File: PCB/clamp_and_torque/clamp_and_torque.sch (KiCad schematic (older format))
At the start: 12 parts, among them J1 Servo1, J2 Servo2, J3 LimitSwitches, J4 Conn_01x02_Female, J5 Conn_01x02_Female

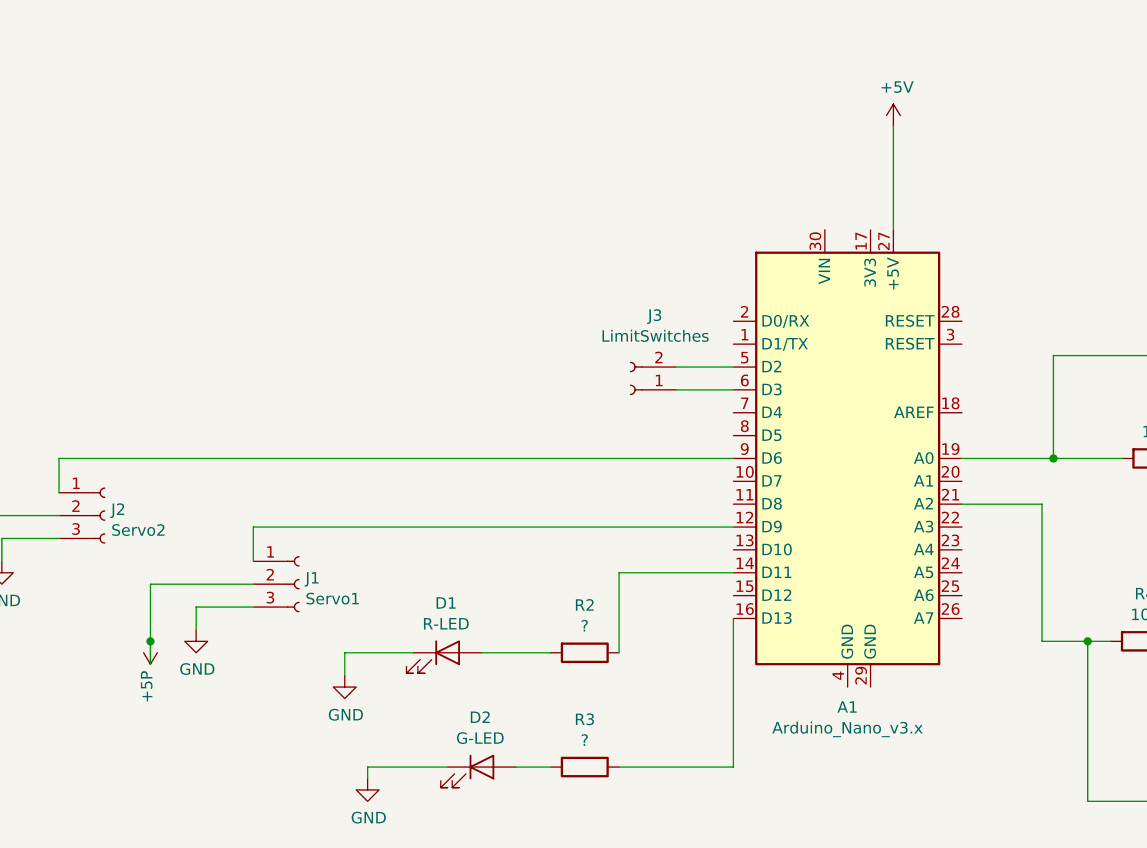
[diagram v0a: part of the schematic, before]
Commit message: Update some footprints and add a few more components.
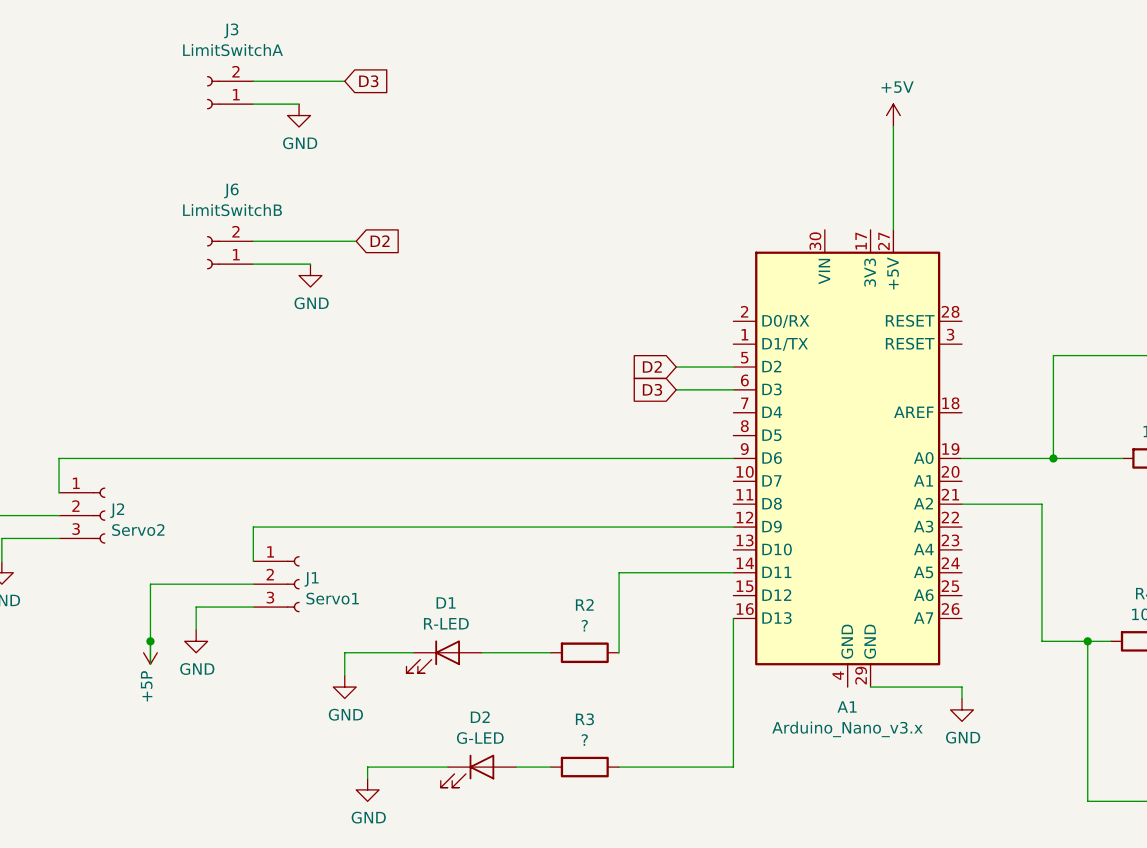
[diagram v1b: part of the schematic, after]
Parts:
- added J6: LimitSwitchB, Connector_PinHeader_2.54mm:PinHeader_1x02_P2.54mm_Vertical, symbol Connector:Conn_01x02_Female
- J1, J2: footprint (none) -> Connector_PinHeader_2.54mm:PinHeader_1x02_P5.04mm_Vertical
- J3: value LimitSwitches -> LimitSwitchA
- J4, J5: footprint (none) -> Connector_PinHeader_2.54mm:PinHeader_1x02_P2.54mm_Vertical_V2
- R1, R4: footprint (none) -> Resistor_SMD:R_0603_1608Metric
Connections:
- net labels added: D2, D3
- wire segments 45 -> 51
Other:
- moved on the sheet: J3
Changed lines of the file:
@@
 EESchema Schematic File Version 4
+LIBS:clamp_and_torque-cache
 EELAYER 30 0
 EELAYER END
@@
 F 0 "R1" V 6243 3550 50  0000 C CNN
 F 1 "10k" V 6334 3550 50  0000 C CNN
-F 2 "" H 6520 3459 50  0000 L CNN
+F 2 "Resistor_SMD:R_0603_1608Metric" H 6520 3459 50  0001 L CNN
 F 3 "~" H 6450 3550 50  0001 C CNN
 	1    6450 3550
@@
 F 0 "J1" H 2728 4126 50  0000 L CNN
 F 1 "Servo1" H 2728 4035 50  0000 L CNN
-F 2 "" H 2700 4100 50  0001 C CNN
+F 2 "Connector_PinHeader_2.54mm:PinHeader_1x02_P5.04mm_Vertical" H 2700 4100 50  0001 C CNN
 F 3 "~" H 2700 4100 50  0001 C CNN
 	1    2700 4100
@@
 F 0 "J4" H 7478 2976 50  0000 L CNN
 F 1 "Conn_01x02_Female" H 7478 2885 50  0000 L CNN
-F 2 "" H 7450 3000 50  0001 C CNN
+F 2 "Connector_PinHeader_2.54mm:PinHeader_1x02_P2.54mm_Vertical_V2" H 7450 3000 50  0001 C CNN
 F 3 "~" H 7450 3000 50  0001 C CNN
 	1    7450 3000
@@
 L Connector:Conn_01x02_Female J3
 U 1 1 5DAFAF0D
-P 4150 3250
-F 0 "J3" H 4042 2925 50  0000 C CNN
-F 1 "LimitSwitches" H 4042 3016 50  0000 C CNN
-F 2 "Connector_PinHeader_2.54mm:PinHeader_1x02_P2.54mm_Vertical" H 4150 3250 50  0001 C CNN
-F 3 "~" H 4150 3250 50  0001 C CNN
-	1    4150 3250
+P 2300 2000
+F 0 "J3" H 2192 1675 50  0000 C CNN
+F 1 "LimitSwitchA" H 2192 1766 50  0000 C CNN
+F 2 "Connector_PinHeader_2.54mm:PinHeader_1x02_P2.54mm_Vertical" H 2300 2000 50  0001 C CNN
+F 3 "~" H 2300 2000 50  0001 C CNN
+	1    2300 2000
 	-1   0    0    1
 $EndComp
@@
 F 0 "J2" H 1878 3826 50  0000 L CNN
 F 1 "Servo2" H 1878 3735 50  0000 L CNN
-F 2 "" H 1850 3800 50  0001 C CNN
+F 2 "Connector_PinHeader_2.54mm:PinHeader_1x02_P5.04mm_Vertical" H 1850 3800 50  0001 C CNN
 F 3 "~" H 1850 3800 50  0001 C CNN
 	1    1850 3800
@@
 F 0 "J5" H 7628 4926 50  0000 L CNN
 F 1 "Conn_01x02_Female" H 7628 4835 50  0000 L CNN
-F 2 "" H 7600 4950 50  0001 C CNN
+F 2 "Connector_PinHeader_2.54mm:PinHeader_1x02_P2.54mm_Vertical_V2" H 7600 4950 50  0001 C CNN
 F 3 "~" H 7600 4950 50  0001 C CNN
 	1    7600 4950
@@
 F 0 "R4" V 6193 4350 50  0000 C CNN
 F 1 "10k" V 6284 4350 50  0000 C CNN
-F 2 "" H 6470 4259 50  0000 L CNN
+F 2 "Resistor_SMD:R_0603_1608Metric" H 6470 4259 50  0001 L CNN
 F 3 "~" H 6400 4350 50  0001 C CNN
 	1    6400 4350
@@
 Wire Wire Line
 	6150 5050 7400 5050
+$Comp
+L Connector:Conn_01x02_Female J6
+U 1 1 5DB0E066
+P 2300 2700
+F 0 "J6" H 2192 2375 50  0000 C CNN
+F 1 "LimitSwitchB" H 2192 2466 50  0000 C CNN
+F 2 "Connector_PinHeader_2.54mm:PinHeader_1x02_P2.54mm_Vertical" H 2300 2700 50  0001 C CNN
+F 3 "~" H 2300 2700 50  0001 C CNN
+	1    2300 2700
+	-1   0    0    1
+$EndComp
+$Comp
+L power:GND #PWR0112
+U 1 1 5DB0EAAF
+P 2700 2000
+F 0 "#PWR0112" H 2700 1750 50  0001 C CNN
+F 1 "GND" H 2705 1827 50  0000 C CNN
+F 2 "" H 2700 2000 50  0001 C CNN
+F 3 "" H 2700 2000 50  0001 C CNN
+	1    2700 2000
+	1    0    0    -1
+$EndComp
+Text GLabel 4350 3150 0    50   Input ~ 0
+D2
+Text GLabel 4350 3250 0    50   Input ~ 0
+D3
+Text GLabel 2950 2600 2    50   Input ~ 0
+D2
+Text GLabel 2900 1900 2    50   Input ~ 0
+D3
+$Comp
+L power:GND #PWR0113
+U 1 1 5DB1DE6D
+P 2750 2700
+F 0 "#PWR0113" H 2750 2450 50  0001 C CNN
+F 1 "GND" H 2755 2527 50  0000 C CNN
+F 2 "" H 2750 2700 50  0001 C CNN
+F 3 "" H 2750 2700 50  0001 C CNN
+	1    2750 2700
+	1    0    0    -1
+$EndComp
+Wire Wire Line
+	2500 2000 2700 2000
+Wire Wire Line
+	2500 1900 2900 1900
+Wire Wire Line
+	2500 2600 2950 2600
+Wire Wire Line
+	2500 2700 2750 2700
+$Comp
+L power:GND #PWR?
+U 1 1 5DB261B3
+P 5600 4600
+F 0 "#PWR?" H 5600 4350 50  0001 C CNN
+F 1 "GND" H 5605 4427 50  0000 C CNN
+F 2 "" H 5600 4600 50  0001 C CNN
+F 3 "" H 5600 4600 50  0001 C CNN
+	1    5600 4600
+	1    0    0    -1
+$EndComp
+Wire Wire Line
+	5200 4550 5600 4550
+Wire Wire Line
+	5600 4550 5600 4600
 $EndSCHEMATC

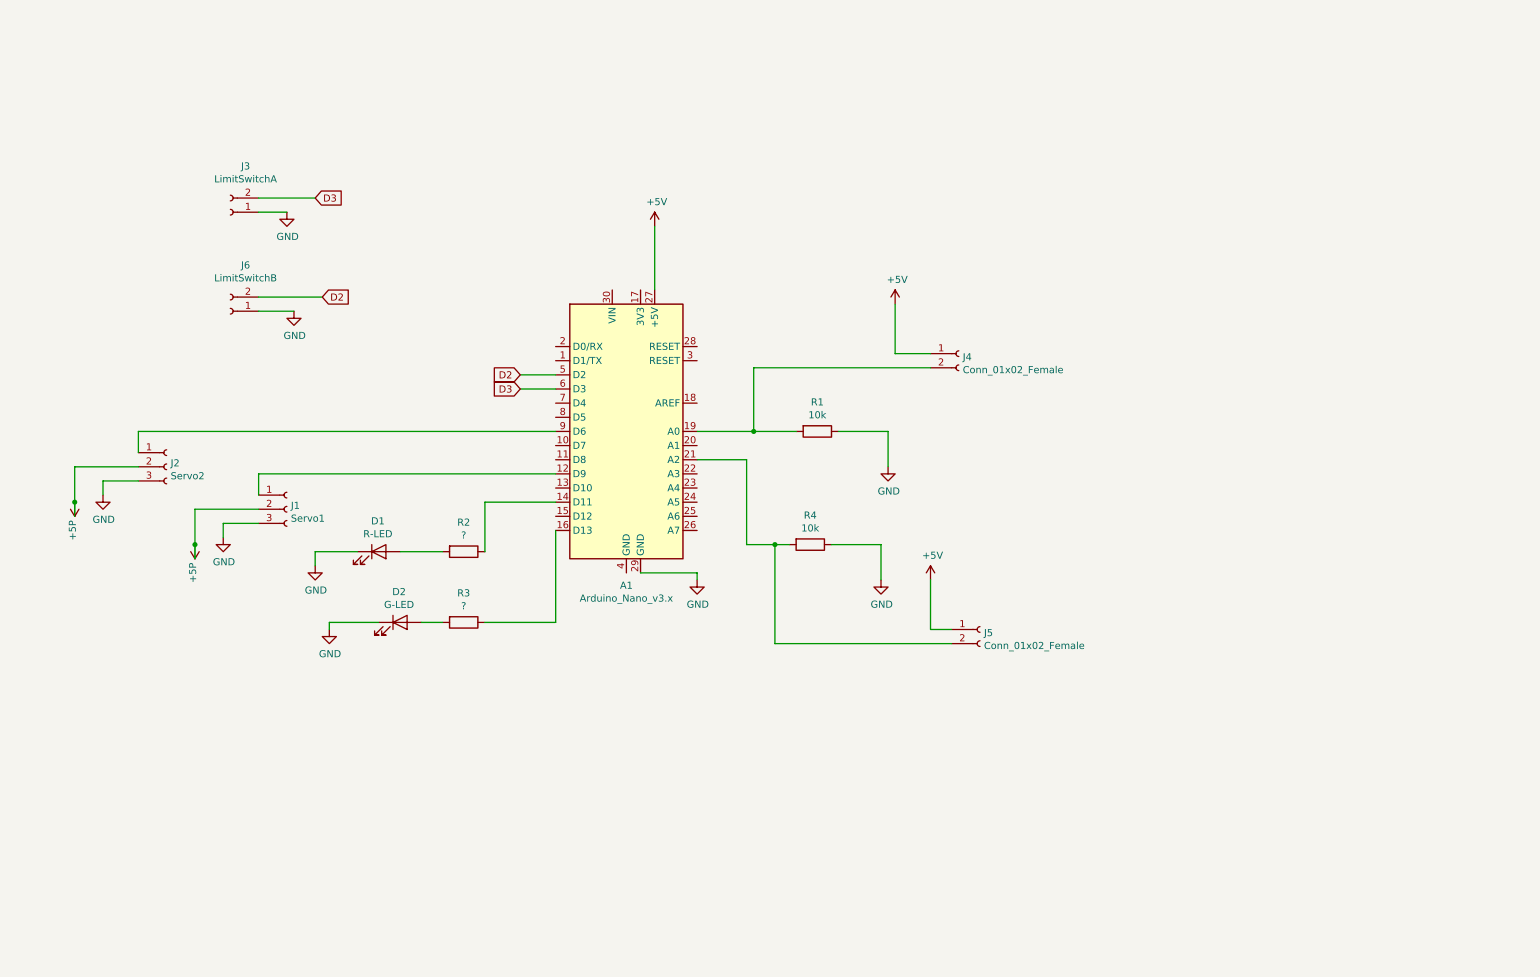
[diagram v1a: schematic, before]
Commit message: Cleaned up schematic and roughly placed all components.
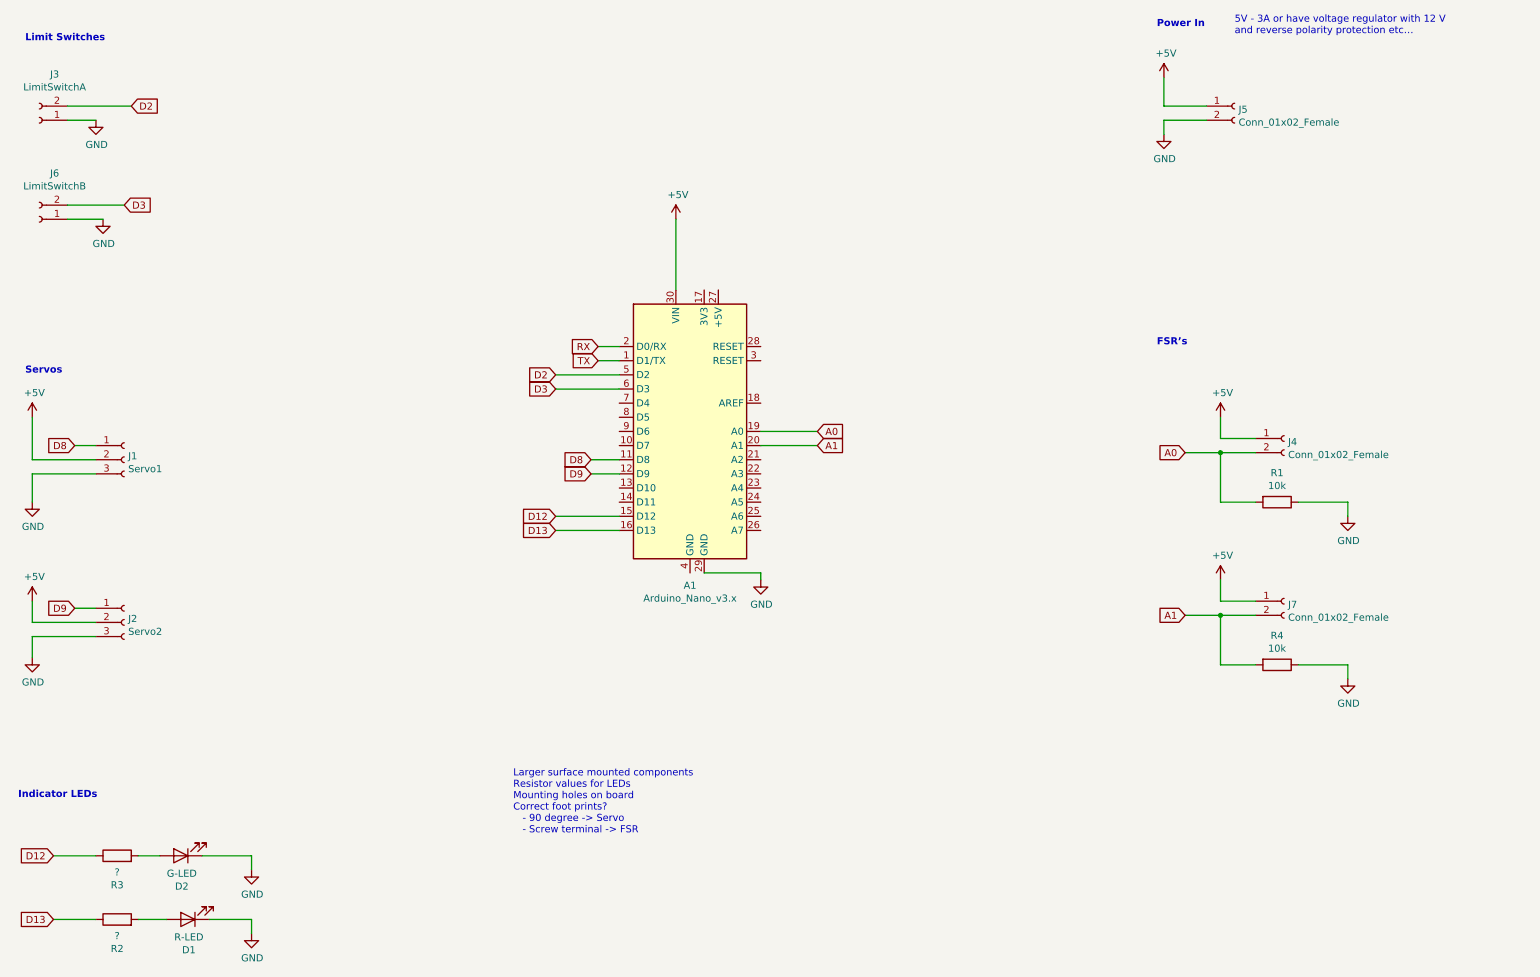
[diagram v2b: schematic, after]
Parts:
- added J7: Conn_01x02_Female, Connector_PinHeader_2.54mm:PinHeader_1x02_P2.54mm_Vertical_V2, symbol Connector:Conn_01x02_Female
- J1, J2: footprint Connector_PinHeader_2.54mm:PinHeader_1x02_P5.04mm_Vertical -> Connector_PinHeader_2.54mm:PinHeader_1x03_P2.54mm_Vertical
- J5: footprint Connector_PinHeader_2.54mm:PinHeader_1x02_P2.54mm_Vertical_V2 -> Connector_PinHeader_2.54mm:PinHeader_1x02_P2.54mm_Vertical
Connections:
- net labels added: A0, A1, D12, D13, D8, D9, RX, TX
- net labels removed: +5P
- wire segments 51 -> 55
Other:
- note added: "5V - 3A or have voltage regulator with 12 V \nand reverse polarity protection etc…"
- note added: "FSR’s"
- note added: "Indicator LEDs"
- note added: "Larger surface mounted components\nResistor values for LEDs\nMounting holes on board\nCorrect foot prints?\n - 90 degree -> Servo\n - Screw terminal -> FSR\n"
- note added: "Limit Switches"
- note added: "Power In"
- note added: "Servos"
- moved on the sheet: A1, D1, D2, J1, J2, J3, J4, J6, R1, R2, R3

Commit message: Add NRF24L01 pinout to PCB
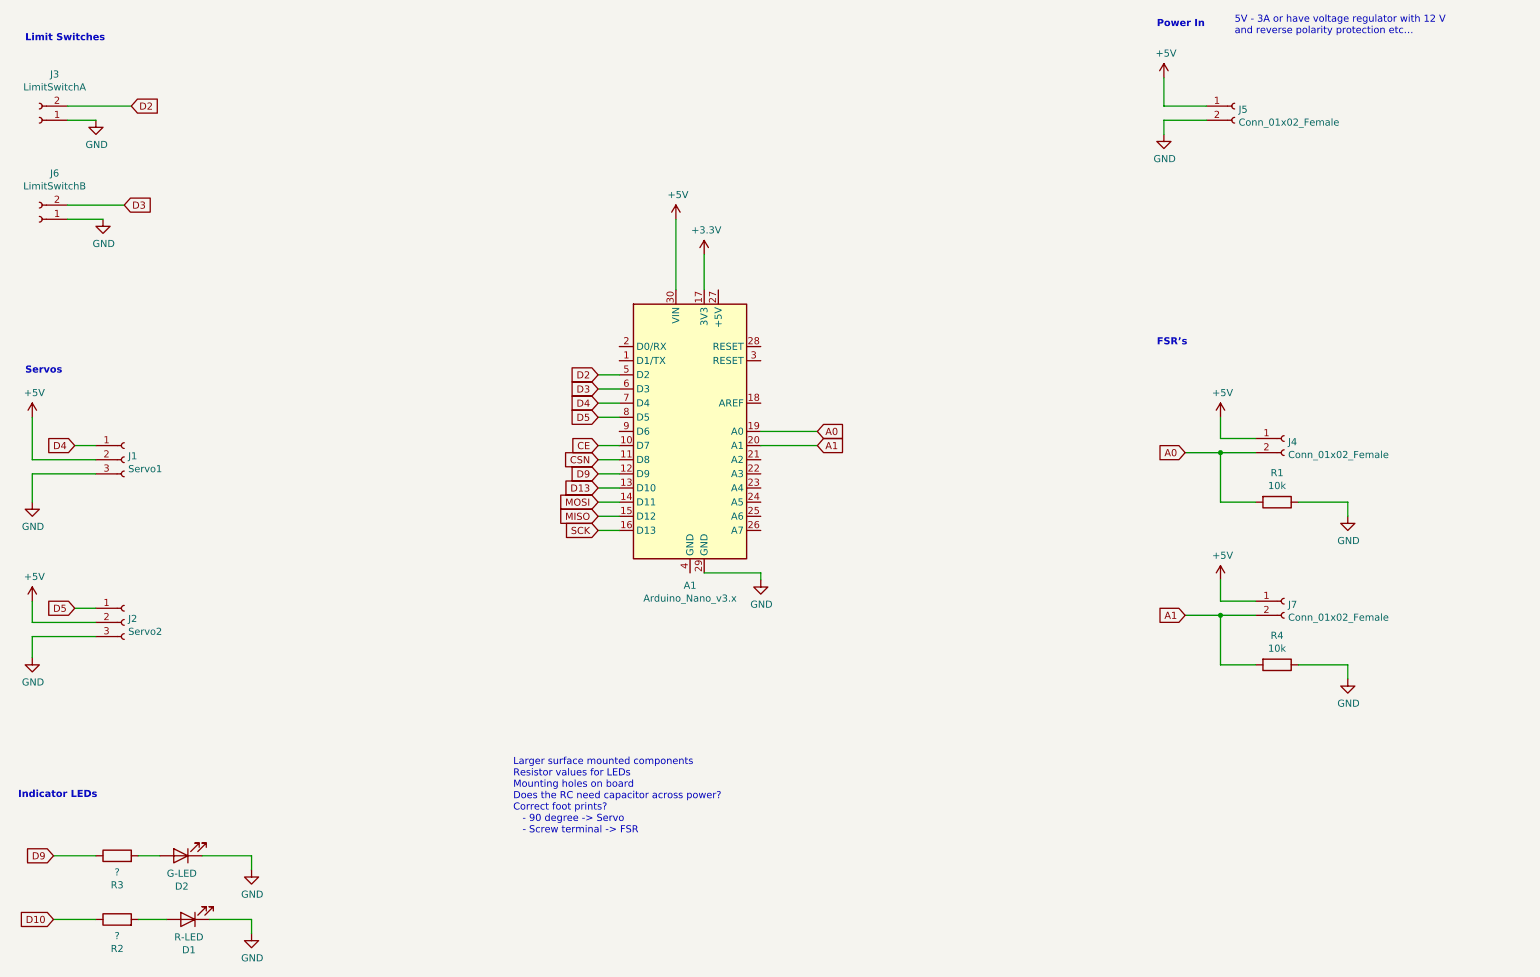
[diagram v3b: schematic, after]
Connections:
- net D13: now also A1.13 (D10); no longer A1.16 (D13), R2.1
- net D9: now also R3.1; no longer J2.1 (Pin_1)
- net CE: now reaches A1.10 (D7)
- net MOSI: now reaches A1.14 (D11)
- net +3V3: now reaches A1.17 (3V3)
- net D4: now reaches A1.7 (D4)
- net D4: now also J1.1 (Pin_1)
- net D5: now reaches A1.8 (D5)
- net D5: now also J2.1 (Pin_1)
- net D12 renamed MISO
- net MISO: no longer R3.1
- net D8 renamed CSN
- net CSN: no longer J1.1 (Pin_1)
- net RX: no longer names the net of A1.2 (D0/RX)
- net TX: no longer names the net of A1.1 (D1/TX)
- new net D10: R2.1
- new net SCK: A1.16 (D13)
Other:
- note added: "Larger surface mounted components\nResistor values for LEDs\nMounting holes on board\nDoes the RC need capacitor across power?\nCorrect foot prints?\n - 90 degree -> Servo\n - Screw terminal -> FSR\n"
- note removed: "Larger surface mounted components\nResistor values for LEDs\nMounting holes on board\nCorrect foot prints?\n - 90 degree -> Servo\n - Screw terminal -> FSR\n"
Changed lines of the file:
@@
 	1    0    0    -1
 $EndComp
-Text GLabel 4600 3150 0    50   Input ~ 0
+Text GLabel 4900 3150 0    50   Input ~ 0
 D2
-Text GLabel 4600 3250 0    50   Input ~ 0
+Text GLabel 4900 3250 0    50   Input ~ 0
 D3
 Text GLabel 1600 1250 2    50   Input ~ 0
@@
 Wire Wire Line
 	5450 2550 5450 2050
-Text GLabel 4900 2950 0    50   Input ~ 0
-RX
-Wire Wire Line
-	4600 3250 5050 3250
-Wire Wire Line
-	4600 3150 5050 3150
-Wire Wire Line
-	4900 2950 5050 2950
-Text GLabel 4900 3050 0    50   Input ~ 0
-TX
-Wire Wire Line
-	5050 3050 4900 3050
 $Comp
 L power:+5V #PWR0111
@@
 Wire Wire Line
 	900  5000 1350 5000
-Text GLabel 4850 3850 0    50   Input ~ 0
-D9
-Text GLabel 4850 3750 0    50   Input ~ 0
-D8
-Wire Wire Line
-	4850 3750 5050 3750
-Wire Wire Line
-	4850 3850 5050 3850
+Text GLabel 4900 3450 0    50   Input ~ 0
+D5
+Text GLabel 4900 3350 0    50   Input ~ 0
+D4
 Text GLabel 1200 3650 0    50   Input ~ 0
-D8
+D4
 Text GLabel 1200 4800 0    50   Input ~ 0
-D9
+D5
 Wire Wire Line
 	1200 4800 1350 4800
@@
 Wire Wire Line
 	2450 6650 2450 6550
-Text GLabel 4600 4150 0    50   Input ~ 0
-D12
-Text GLabel 4600 4250 0    50   Input ~ 0
+Text GLabel 4900 3850 0    50   Input ~ 0
+D9
+Text GLabel 4900 3950 0    50   Input ~ 0
 D13
-Wire Wire Line
-	4600 4150 5050 4150
-Wire Wire Line
-	4600 4250 5050 4250
 Text GLabel 1050 6550 0    50   Input ~ 0
-D12
+D9
 Text GLabel 1050 7000 0    50   Input ~ 0
-D13
+D10
 Wire Wire Line
 	1050 6550 1350 6550
@@
 Indicator LEDs
 Text Notes 4300 6400 0    50   ~ 0
-Larger surface mounted components\nResistor values for LEDs\nMounting holes on board\nCorrect foot prints?\n   - 90 degree -> Servo\n   - Screw terminal -> FSR\n
+Larger surface mounted components\nResistor values for LEDs\nMounting holes on board\nDoes the RC need capacitor across power?\nCorrect foot prints?\n   - 90 degree -> Servo\n   - Screw terminal -> FSR\n
+$Comp
+L power:+3.3V #PWR?
+U 1 1 5DB748D2
+P 5650 2300
+F 0 "#PWR?" H 5650 2150 50  0001 C CNN
+F 1 "+3.3V" H 5665 2473 50  0000 C CNN
+F 2 "" H 5650 2300 50  0001 C CNN
+F 3 "" H 5650 2300 50  0001 C CNN
+	1    5650 2300
+	1    0    0    -1
+$EndComp
+Wire Wire Line
+	5650 2550 5650 2300
+Wire Wire Line
+	4900 3350 5050 3350
+Wire Wire Line
+	4900 3450 5050 3450
+Text GLabel 4900 3650 0    50   Input ~ 0
+CE
+Text GLabel 4900 3750 0    50   Input ~ 0
+CSN
+Text GLabel 4900 4250 0    50   Input ~ 0
+SCK
+Text GLabel 4900 4050 0    50   Input ~ 0
+MOSI
+Text GLabel 4900 4150 0    50   Input ~ 0
+MISO
+Wire Wire Line
+	4900 3250 5050 3250
+Wire Wire Line
+	4900 3150 5050 3150
+Wire Wire Line
+	4900 3650 5050 3650
+Wire Wire Line
+	4900 3750 5050 3750
+Wire Wire Line
+	4900 4050 5050 4050
+Wire Wire Line
+	4900 4150 5050 4150
+Wire Wire Line
+	4900 4250 5050 4250
+Wire Wire Line
+	4900 3850 5050 3850
+Wire Wire Line
+	4900 3950 5050 3950
 $EndSCHEMATC
